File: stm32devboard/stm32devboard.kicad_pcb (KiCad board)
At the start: 4 copper layers, 20.3 x 61 mm, 44 parts, among them J1 Conn_01x20, J2 Conn_01x20, J3 USB_C_Receptacle_USB2.0, J4 ARM_SWD_TagConnect_TC2030-NL, SW1 SW_SPST, SW2 SW_SPST, U1 STM32F042C6Tx, U2 AP63203WU, U3 TCAN332, U4 IP4234CZ6,125, X1 ECS-160-10-36Q-ES-TR

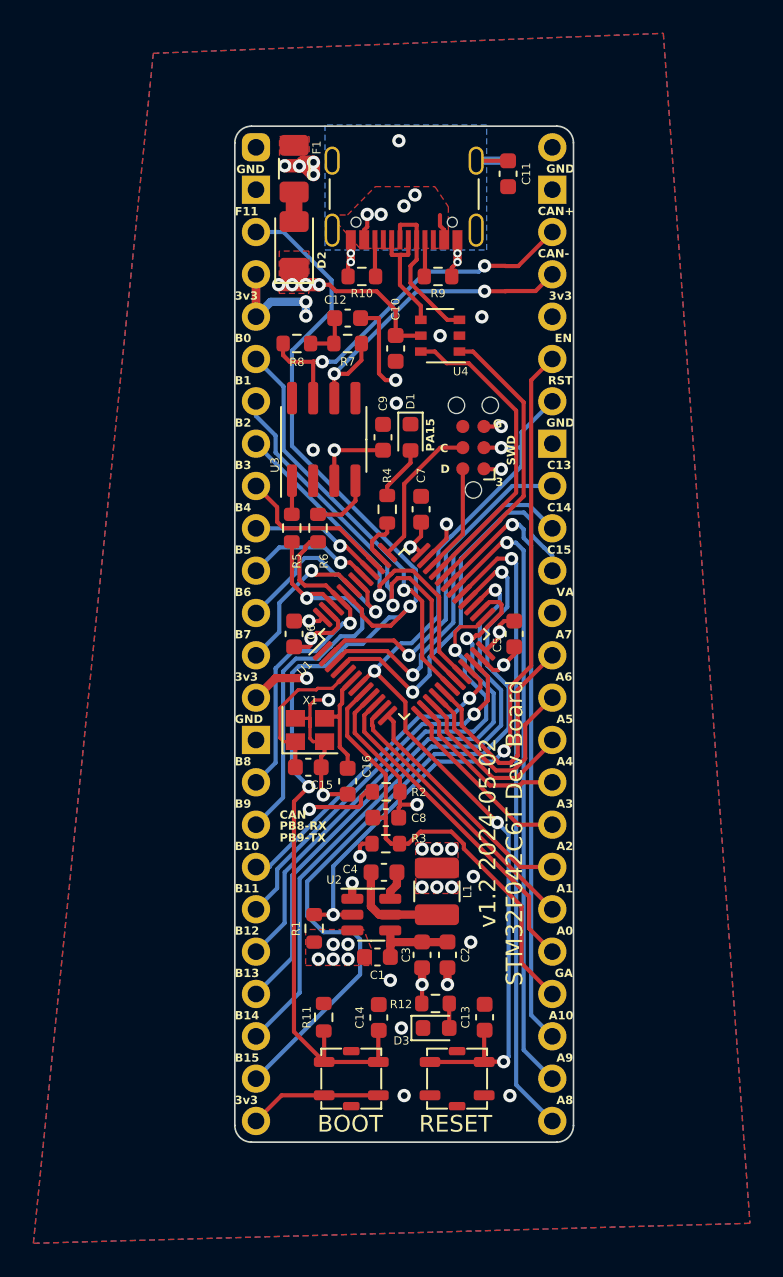
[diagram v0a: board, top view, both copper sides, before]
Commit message: Fix for TVS diode to be set to <=5V
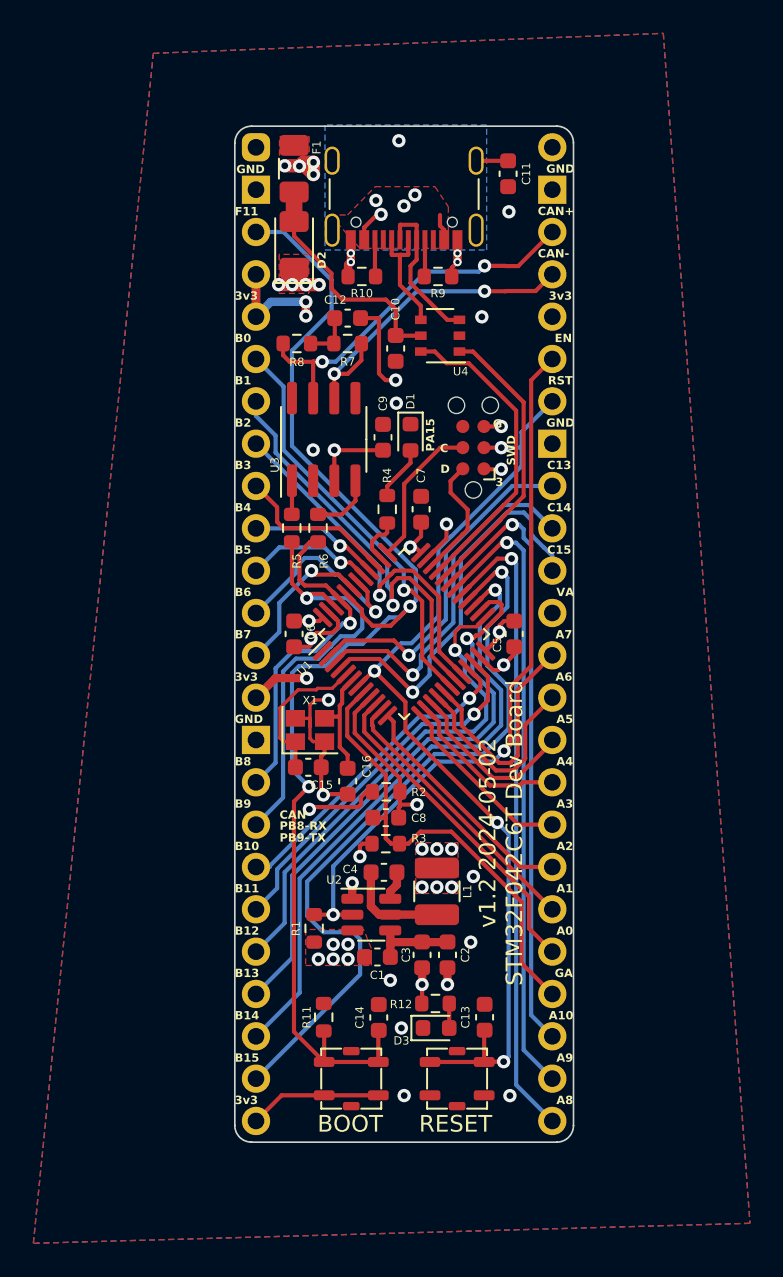
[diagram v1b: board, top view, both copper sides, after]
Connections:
- C10 pad 1: VBUS -> Net-(D2-A)
- U4 pad 5: VBUS -> Net-(D2-A)
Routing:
- net Net-(D2-A): track 1.52 -> 13.9 mm
- net VBUS: track 74.9 -> 66.6 mm
- net /USB_SHLD: track 3.74 -> 2.00 mm
- net /SWDIO: track 6.47 -> 7.34 mm

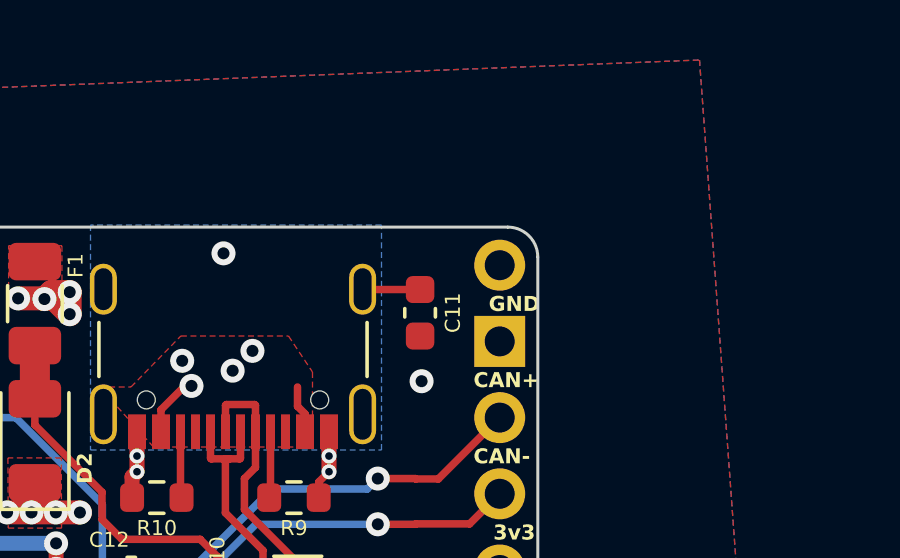
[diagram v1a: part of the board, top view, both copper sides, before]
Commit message: added VBUS label
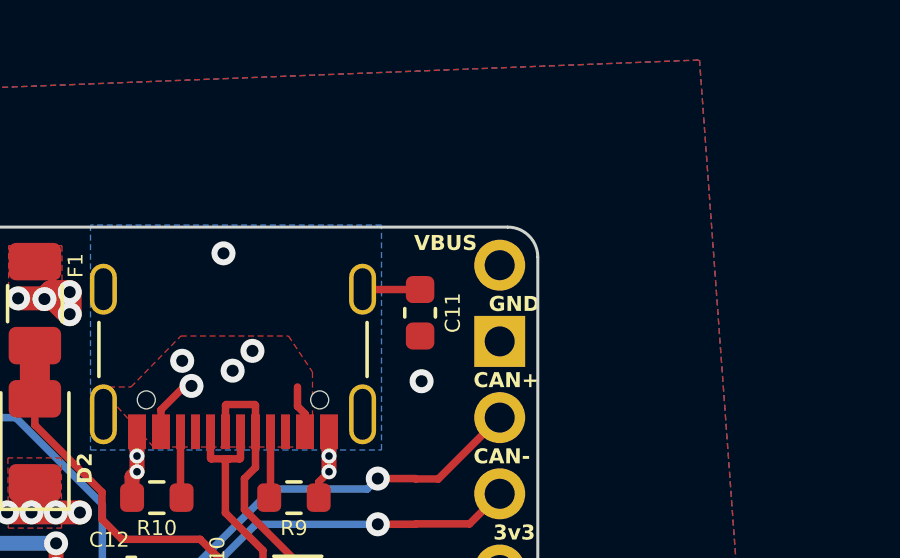
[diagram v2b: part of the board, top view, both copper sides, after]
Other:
- board text added: "VBUS"
